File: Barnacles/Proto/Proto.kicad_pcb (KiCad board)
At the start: 2 copper layers, 82.6 x 17.3 mm, 16 parts, among them J1 Conn_01x01, J1 Conn_02x35_Top_Bottom, J12 Conn_02x03_Top_Bottom, J13 Conn_02x03_Top_Bottom, J2 Conn_01x01, J3 Conn_01x01, J4 Conn_01x01, J5 Conn_01x01, J6 Conn_02x35_Top_Bottom

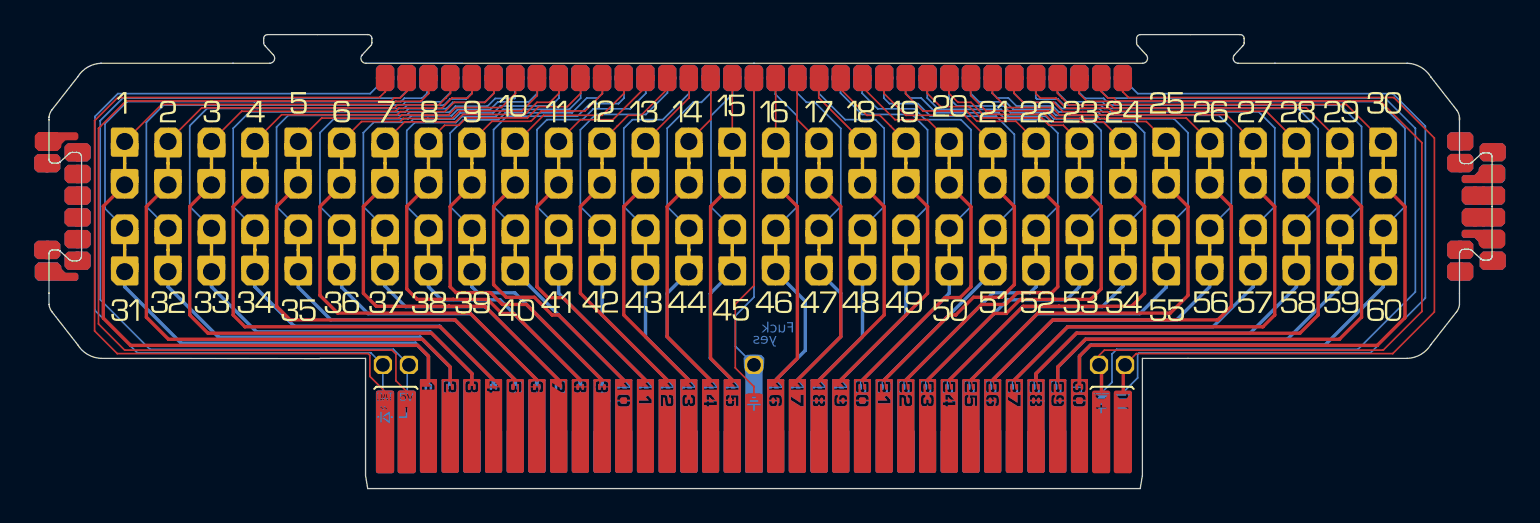
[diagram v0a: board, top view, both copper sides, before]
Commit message: actually route most of the barnacles
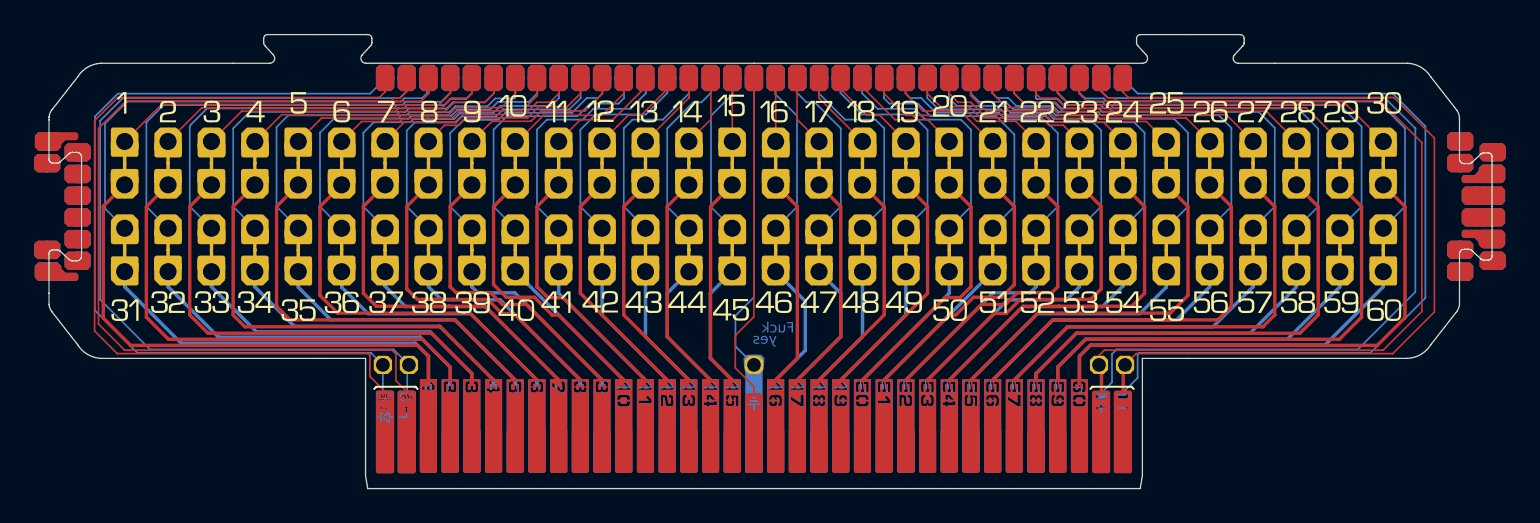
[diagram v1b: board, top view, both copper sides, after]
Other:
- board size 82.6 x 17.3 mm -> 82.5 x 17.3 mm
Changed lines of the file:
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@@
 	)
 	(gr_line
-		(start 129.791253 68.723681)
+		(start 129.791253 68.706999)
 		(end 116.982054 68.707001)
 		(stroke
@@
 	)
 	(gr_line
-		(start 180.591253 68.707001)
-		(end 193.432968 68.707001)
+		(start 180.591253 68.707)
+		(end 193.43247 68.707001)
 		(stroke
 			(width 0.05)
@@
 	)
 	(gr_line
-		(start 196.481253 54.584601)
-		(end 196.481253 54.753513)
+		(start 196.481253 54.644121)
+		(end 196.481253 54.737044)
 		(stroke
 			(width 0.05)
@@
 	(gr_line
 		(start 196.481253 64.897044)
-		(end 196.481271 65.551506)
+		(end 196.481271 65.551498)
 		(stroke
 			(width 0.05)
@@
 	)
 	(gr_line
-		(start 113.934038 64.897044)
-		(end 113.934036 65.55146)
+		(start 113.934038 64.902001)
+		(end 113.934027 65.551464)
 		(stroke
 			(width 0.05)
@@
 	)
 	(gr_line
-		(start 113.934038 54.737001)
-		(end 113.934038 54.590304)
+		(start 113.934038 54.742001)
+		(end 113.934038 54.590314)
 		(stroke
 			(width 0.05)
@@
 	(gr_arc
 		(start 196.313817 54.166033)
-		(mid 196.453395 54.443855)
-		(end 196.481253 54.753513)
+		(mid 196.435688 54.391715)
+		(end 196.481253 54.644121)
 		(stroke
 			(width 0.05)
@@
 	)
 	(segment
-		(start 155.191252 70.358)
-		(end 154.099053 69.265801)
+		(start 155.191252 70.866001)
+		(end 155.191252 70.358)
 		(width 0.1)
 		(layer "F.Cu")
@@
 	)
 	(segment
-		(start 154.099053 69.265801)
-		(end 154.099053 65.532001)
+		(start 155.191253 66.2722)
+		(end 155.191253 52.341001)
 		(width 0.1)
 		(layer "F.Cu")
@@
 	)
 	(segment
-		(start 155.191253 52.341001)
-		(end 155.174253 52.324001)
+		(start 155.191252 70.358)
+		(end 154.099053 69.265801)
 		(width 0.1)
 		(layer "F.Cu")
@@
 	)
 	(segment
-		(start 155.191252 70.866001)
-		(end 155.191252 70.358)
+		(start 155.191253 52.341001)
+		(end 155.174253 52.324001)
 		(width 0.1)
 		(layer "F.Cu")
@@
 	)
 	(segment
-		(start 155.191253 64.439801)
-		(end 155.191253 52.341001)
+		(start 154.099053 67.3644)
+		(end 155.191253 66.2722)
 		(width 0.1)
 		(layer "F.Cu")
@@
 	)
 	(segment
-		(start 154.099053 65.532001)
-		(end 155.191253 64.439801)
+		(start 154.099053 69.265801)
+		(end 154.099053 67.3644)
 		(width 0.1)
 		(layer "F.Cu")
